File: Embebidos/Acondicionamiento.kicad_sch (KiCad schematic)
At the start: 20 parts

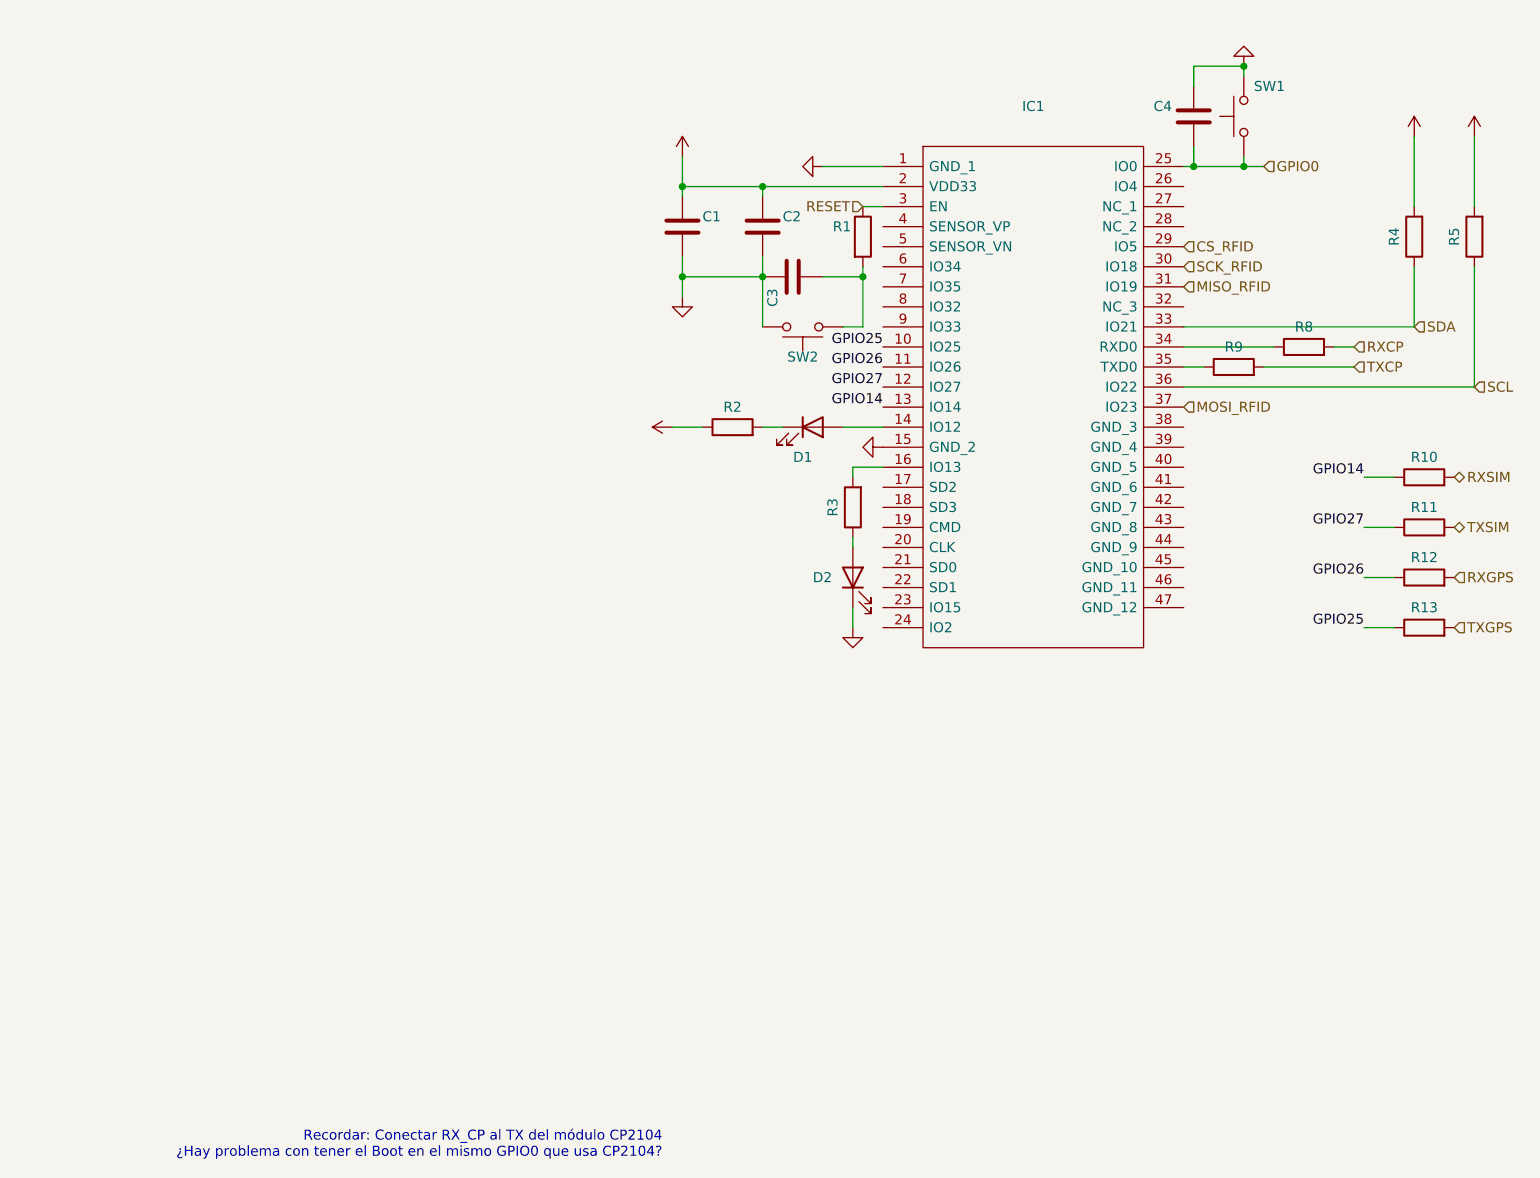
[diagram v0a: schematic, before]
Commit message: LDR module adittion
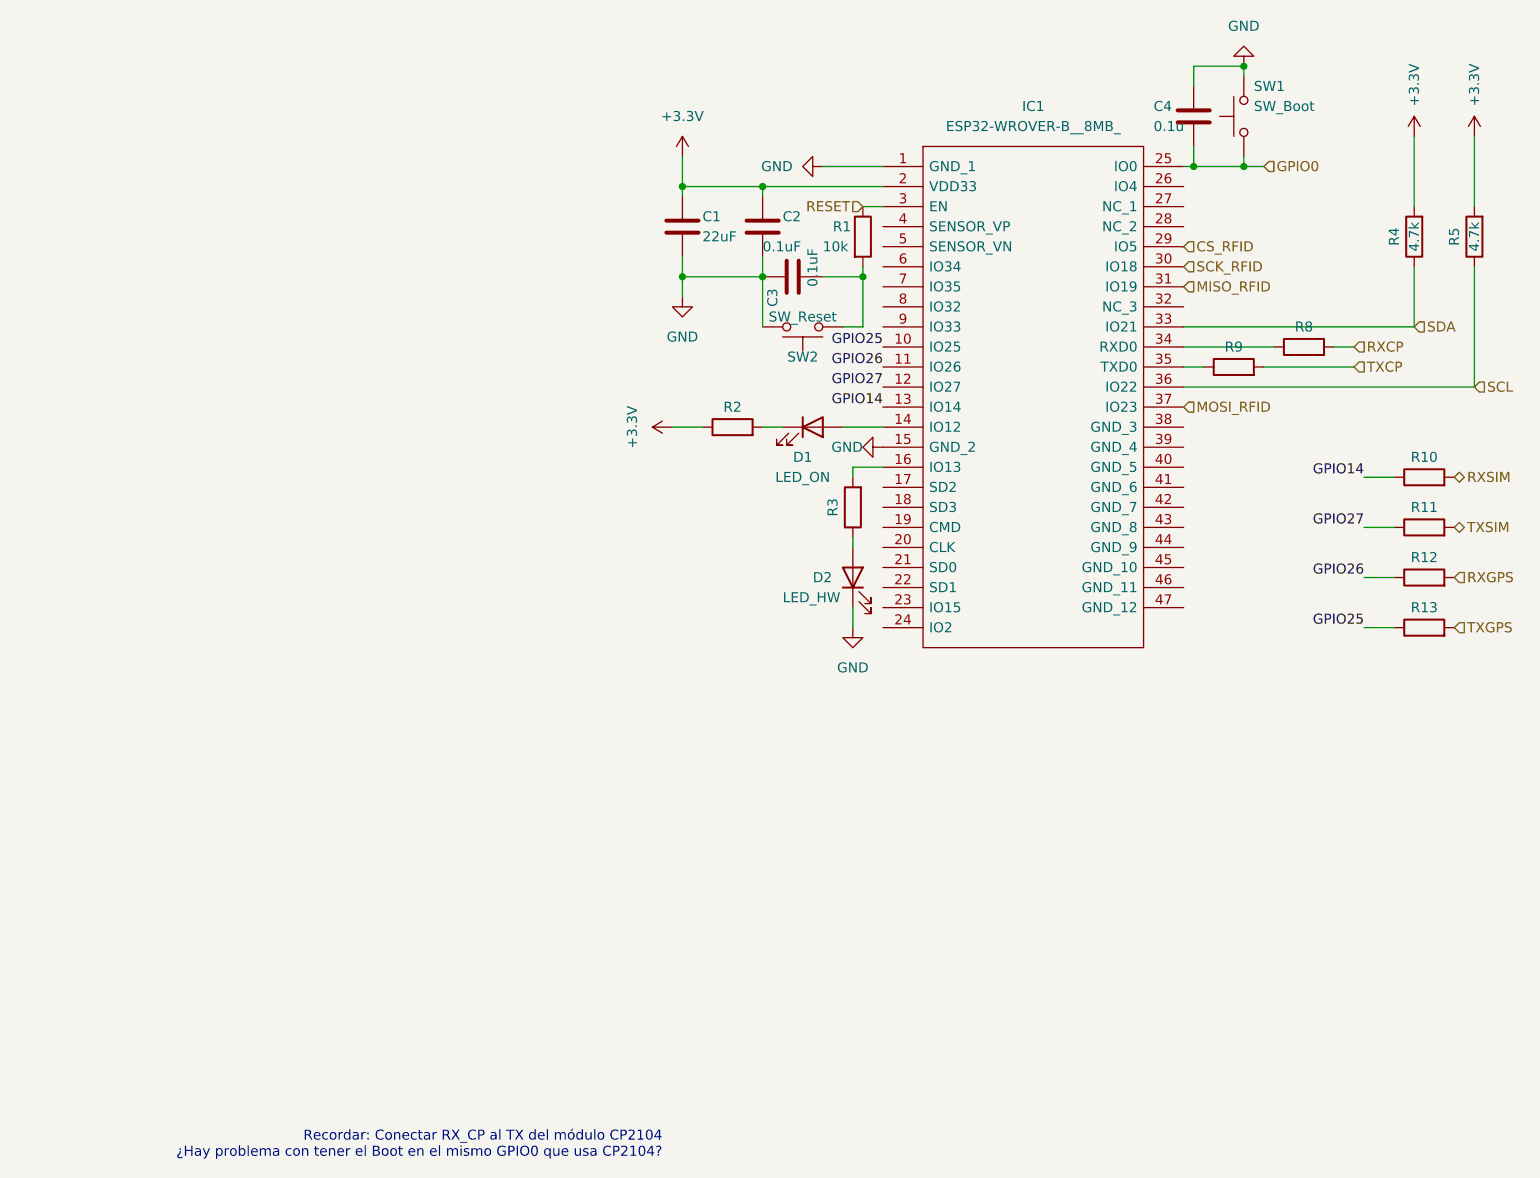
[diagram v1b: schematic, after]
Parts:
- C1: value (none) -> 22uF
- C2, C3: value (none) -> 0.1uF
- C4: value (none) -> 0.1u
- D1: value (none) -> LED_ON
- D2: value (none) -> LED_HW
- IC1: value (none) -> ESP32-WROVER-B__8MB_; footprint (none) -> ESP32WROVERB8MB
- R1: value (none) -> 10k
- R4, R5: value (none) -> 4.7k
- SW1: value (none) -> SW_Boot
- SW2: value (none) -> SW_Reset
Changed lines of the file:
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@@
       (effects (font (size 1.27 1.27)) (justify left))
     )
-    (property "Value" "" (id 1) (at 106.68 78.74 0)
+    (property "Value" "10k" (id 1) (at 106.68 78.74 0)
       (effects (font (size 1.27 1.27)) (justify left))
     )
@@
       (effects (font (size 1.27 1.27)) (justify left))
     )
-    (property "Value" "" (id 1) (at 105.41 83.82 0)
+    (property "Value" "0.1uF" (id 1) (at 105.41 83.82 0)
       (effects (font (size 1.27 1.27)) (justify left))
     )
@@
       (effects (font (size 1.27 1.27)) (justify left))
     )
-    (property "Value" "" (id 1) (at 99.06 78.74 0)
+    (property "Value" "0.1uF" (id 1) (at 99.06 78.74 0)
       (effects (font (size 1.27 1.27)) (justify left))
     )
@@
       (effects (font (size 1.27 1.27)) hide)
     )
-    (property "Value" "" (id 1) (at 88.9 90.17 0))
+    (property "Value" "GND" (id 1) (at 88.9 90.17 0))
     (property "Footprint" "" (id 2) (at 88.9 85.09 0)
       (effects (font (size 1.27 1.27)) hide)
@@
       (effects (font (size 1.27 1.27)) hide)
     )
-    (property "Value" "" (id 1) (at 160.02 50.8 0))
+    (property "Value" "GND" (id 1) (at 160.02 50.8 0))
     (property "Footprint" "" (id 2) (at 160.02 55.88 0)
       (effects (font (size 1.27 1.27)) hide)
@@
       (effects (font (size 1.27 1.27)) hide)
     )
-    (property "Value" "" (id 1) (at 111.76 104.14 90)
+    (property "Value" "GND" (id 1) (at 111.76 104.14 90)
       (effects (font (size 1.27 1.27)) (justify right))
     )
@@
       (effects (font (size 1.27 1.27)) hide)
     )
-    (property "Value" "" (id 1) (at 181.6099 60.96 90)
+    (property "Value" "+3.3V" (id 1) (at 181.6099 60.96 90)
       (effects (font (size 1.27 1.27)) (justify left))
     )
@@
       (effects (font (size 1.27 1.27)) (justify left))
     )
-    (property "Value" "" (id 1) (at 148.59 63.5 0)
+    (property "Value" "0.1u" (id 1) (at 148.59 63.5 0)
       (effects (font (size 1.27 1.27)) (justify left))
     )
@@
       (effects (font (size 1.27 1.27)) hide)
     )
-    (property "Value" "" (id 1) (at 88.9 62.23 0))
+    (property "Value" "+3.3V" (id 1) (at 88.9 62.23 0))
     (property "Footprint" "" (id 2) (at 88.9 67.31 0)
       (effects (font (size 1.27 1.27)) hide)
@@
       (effects (font (size 1.27 1.27)) (justify right))
     )
-    (property "Value" "" (id 1) (at 161.29 60.96 90)
+    (property "Value" "SW_Boot" (id 1) (at 161.29 60.96 90)
       (effects (font (size 1.27 1.27)) (justify right))
     )
@@
       (effects (font (size 1.27 1.27)) hide)
     )
-    (property "Value" "" (id 1) (at 189.2299 60.96 90)
+    (property "Value" "+3.3V" (id 1) (at 189.2299 60.96 90)
       (effects (font (size 1.27 1.27)) (justify left))
     )
@@
     (in_bom yes) (on_board yes)
     (property "Reference" "R4" (id 0) (at 179.07 77.47 90))
-    (property "Value" "" (id 1) (at 181.61 77.47 90))
+    (property "Value" "4.7k" (id 1) (at 181.61 77.47 90))
     (property "Footprint" "" (id 2) (at 183.388 77.47 90)
       (effects (font (size 1.27 1.27)) hide)
@@
       (effects (font (size 1.27 1.27)) hide)
     )
-    (property "Value" "" (id 1) (at 82.55 101.6 0))
+    (property "Value" "+3.3V" (id 1) (at 82.55 101.6 0))
     (property "Footprint" "" (id 2) (at 87.63 101.6 0)
       (effects (font (size 1.27 1.27)) hide)
@@
     (in_bom yes) (on_board yes)
     (property "Reference" "D1" (id 0) (at 104.14 105.41 0))
-    (property "Value" "" (id 1) (at 104.14 107.95 0))
+    (property "Value" "LED_ON" (id 1) (at 104.14 107.95 0))
     (property "Footprint" "" (id 2) (at 105.41 101.6 0)
       (effects (font (size 1.27 1.27)) hide)
@@
     (in_bom yes) (on_board yes)
     (property "Reference" "SW2" (id 0) (at 104.14 92.71 0))
-    (property "Value" "" (id 1) (at 104.14 87.63 0))
+    (property "Value" "SW_Reset" (id 1) (at 104.14 87.63 0))
     (property "Footprint" "" (id 2) (at 104.14 93.98 0)
       (effects (font (size 1.27 1.27)) hide)
@@
     (in_bom yes) (on_board yes) (fields_autoplaced)
     (property "Reference" "IC1" (id 0) (at 133.35 60.96 0))
-    (property "Value" "" (id 1) (at 133.35 63.5 0))
-    (property "Footprint" "" (id 2) (at 148.59 66.04 0)
+    (property "Value" "ESP32-WROVER-B__8MB_" (id 1) (at 133.35 63.5 0))
+    (property "Footprint" "ESP32WROVERB8MB" (id 2) (at 148.59 66.04 0)
       (effects (font (size 1.27 1.27)) (justify left) hide)
     )
@@
       (effects (font (size 1.27 1.27)) (justify left))
     )
-    (property "Value" "" (id 1) (at 91.44 77.47 0)
+    (property "Value" "22uF" (id 1) (at 91.44 77.47 0)
       (effects (font (size 1.27 1.27)) (justify left))
     )
@@
       (effects (font (size 1.27 1.27)) hide)
     )
-    (property "Value" "" (id 1) (at 102.87 68.5799 90)
+    (property "Value" "GND" (id 1) (at 102.87 68.5799 90)
       (effects (font (size 1.27 1.27)) (justify right))
     )
@@
     (in_bom yes) (on_board yes)
     (property "Reference" "R5" (id 0) (at 186.69 77.47 90))
-    (property "Value" "" (id 1) (at 189.23 77.47 90))
+    (property "Value" "4.7k" (id 1) (at 189.23 77.47 90))
     (property "Footprint" "" (id 2) (at 191.008 77.47 90)
       (effects (font (size 1.27 1.27)) hide)
@@
       (effects (font (size 1.27 1.27)) hide)
     )
-    (property "Value" "" (id 1) (at 110.49 132.08 0))
+    (property "Value" "GND" (id 1) (at 110.49 132.08 0))
     (property "Footprint" "" (id 2) (at 110.49 127 0)
       (effects (font (size 1.27 1.27)) hide)
@@
       (effects (font (size 1.27 1.27)) (justify right))
     )
-    (property "Value" "" (id 1) (at 101.6 123.19 90)
-      (effects (font (size 1.27 1.27)) (justify right))
-    )
+    (property "Value" "LED_HW" (id 1) (at 101.6 123.19 90)
+      (effects (font (size 1.27 1.27)) (justify right))
+    )

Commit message: Corrección de anotaciones
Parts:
- renumbered R2 to R1, R13 to R10, R5 to R11, R3 to R2, R1 to R3, R9 to R4, R8 to R5, R4 to R6, R10 to R7, R11 to R8, R12 to R9, SW2 to SW1, SW1 to SW2
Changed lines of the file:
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@@
   (symbol (lib_id "Device:R") (at 111.76 77.47 0) (unit 1)
     (in_bom yes) (on_board yes)
-    (property "Reference" "R1" (id 0) (at 107.95 76.2 0)
+    (property "Reference" "R3" (id 0) (at 107.95 76.2 0)
       (effects (font (size 1.27 1.27)) (justify left))
     )
@@
   (symbol (lib_id "Device:R") (at 158.75 93.98 90) (unit 1)
     (in_bom yes) (on_board yes)
-    (property "Reference" "R9" (id 0) (at 158.75 91.44 90))
+    (property "Reference" "R4" (id 0) (at 158.75 91.44 90))
     (property "Value" "~" (id 1) (at 158.75 93.98 90))
     (property "Footprint" "" (id 2) (at 158.75 95.758 90)
@@
   (symbol (lib_id "Device:R") (at 167.64 91.44 90) (unit 1)
     (in_bom yes) (on_board yes)
-    (property "Reference" "R8" (id 0) (at 167.64 88.9 90))
+    (property "Reference" "R5" (id 0) (at 167.64 88.9 90))
     (property "Value" "~" (id 1) (at 167.64 91.44 90))
     (property "Footprint" "" (id 2) (at 167.64 93.218 90)
@@
   (symbol (lib_id "Device:R") (at 110.49 111.76 180) (unit 1)
     (in_bom yes) (on_board yes)
-    (property "Reference" "R3" (id 0) (at 107.95 111.76 90))
+    (property "Reference" "R2" (id 0) (at 107.95 111.76 90))
     (property "Value" "~" (id 1) (at 110.49 111.76 90))
     (property "Footprint" "" (id 2) (at 112.268 111.76 90)
@@
   (symbol (lib_id "Device:R") (at 95.25 101.6 90) (unit 1)
     (in_bom yes) (on_board yes)
-    (property "Reference" "R2" (id 0) (at 95.25 99.06 90))
+    (property "Reference" "R1" (id 0) (at 95.25 99.06 90))
     (property "Value" "~" (id 1) (at 95.25 101.6 90))
     (property "Footprint" "" (id 2) (at 95.25 103.378 90)
@@
   (symbol (lib_id "power:GND") (at 88.9 85.09 0) (unit 1)
     (in_bom yes) (on_board yes) (fields_autoplaced)
-    (property "Reference" "#PWR?" (id 0) (at 88.9 91.44 0)
+    (property "Reference" "#PWR03" (id 0) (at 88.9 91.44 0)
       (effects (font (size 1.27 1.27)) hide)
     )
@@
   (symbol (lib_id "power:GND") (at 160.02 55.88 180) (unit 1)
     (in_bom yes) (on_board yes)
-    (property "Reference" "#PWR?" (id 0) (at 160.02 49.53 0)
+    (property "Reference" "#PWR07" (id 0) (at 160.02 49.53 0)
       (effects (font (size 1.27 1.27)) hide)
     )
@@
   (symbol (lib_id "power:GND") (at 114.3 104.14 270) (unit 1)
     (in_bom yes) (on_board yes)
-    (property "Reference" "#PWR?" (id 0) (at 107.95 104.14 0)
+    (property "Reference" "#PWR06" (id 0) (at 107.95 104.14 0)
       (effects (font (size 1.27 1.27)) hide)
     )
@@
   (symbol (lib_id "power:+3.3V") (at 181.61 64.77 0) (unit 1)
     (in_bom yes) (on_board yes)
-    (property "Reference" "#PWR?" (id 0) (at 181.61 68.58 0)
+    (property "Reference" "#PWR08" (id 0) (at 181.61 68.58 0)
       (effects (font (size 1.27 1.27)) hide)
     )
@@
   (symbol (lib_id "power:+3.3V") (at 88.9 67.31 0) (unit 1)
     (in_bom yes) (on_board yes) (fields_autoplaced)
-    (property "Reference" "#PWR?" (id 0) (at 88.9 71.12 0)
+    (property "Reference" "#PWR02" (id 0) (at 88.9 71.12 0)
       (effects (font (size 1.27 1.27)) hide)
     )
@@
   (symbol (lib_id "Switch:SW_Push") (at 160.02 62.23 90) (unit 1)
     (in_bom yes) (on_board yes)
-    (property "Reference" "SW1" (id 0) (at 161.29 58.42 90)
+    (property "Reference" "SW2" (id 0) (at 161.29 58.42 90)
       (effects (font (size 1.27 1.27)) (justify right))
     )
@@
   (symbol (lib_id "power:+3.3V") (at 189.23 64.77 0) (unit 1)
     (in_bom yes) (on_board yes) (fields_autoplaced)
-    (property "Reference" "#PWR?" (id 0) (at 189.23 68.58 0)
+    (property "Reference" "#PWR09" (id 0) (at 189.23 68.58 0)
       (effects (font (size 1.27 1.27)) hide)
     )
@@
   (symbol (lib_id "Device:R") (at 181.61 77.47 180) (unit 1)
     (in_bom yes) (on_board yes)
-    (property "Reference" "R4" (id 0) (at 179.07 77.47 90))
+    (property "Reference" "R6" (id 0) (at 179.07 77.47 90))
     (property "Value" "4.7k" (id 1) (at 181.61 77.47 90))
     (property "Footprint" "" (id 2) (at 183.388 77.47 90)
@@
   (symbol (lib_id "power:+3.3V") (at 87.63 101.6 90) (unit 1)
     (in_bom yes) (on_board yes)
-    (property "Reference" "#PWR?" (id 0) (at 91.44 101.6 0)
+    (property "Reference" "#PWR01" (id 0) (at 91.44 101.6 0)
       (effects (font (size 1.27 1.27)) hide)
     )
@@
   (symbol (lib_id "Device:R") (at 182.88 120.65 90) (unit 1)
     (in_bom yes) (on_board yes)
-    (property "Reference" "R12" (id 0) (at 182.88 118.11 90))
+    (property "Reference" "R9" (id 0) (at 182.88 118.11 90))
     (property "Value" "~" (id 1) (at 182.88 120.65 90))
     (property "Footprint" "" (id 2) (at 182.88 122.428 90)
@@
   (symbol (lib_id "Switch:SW_MEC_5G") (at 104.14 88.9 180) (unit 1)
     (in_bom yes) (on_board yes)
-    (property "Reference" "SW2" (id 0) (at 104.14 92.71 0))
+    (property "Reference" "SW1" (id 0) (at 104.14 92.71 0))
     (property "Value" "SW_Reset" (id 1) (at 104.14 87.63 0))
     (property "Footprint" "" (id 2) (at 104.14 93.98 0)
@@
   (symbol (lib_id "Device:R") (at 182.88 107.95 90) (unit 1)
     (in_bom yes) (on_board yes)
-    (property "Reference" "R10" (id 0) (at 182.88 105.41 90))
+    (property "Reference" "R7" (id 0) (at 182.88 105.41 90))
     (property "Value" "~" (id 1) (at 182.88 107.95 90))
     (property "Footprint" "" (id 2) (at 182.88 109.728 90)
@@
   (symbol (lib_id "power:GND") (at 106.68 68.58 270) (unit 1)
     (in_bom yes) (on_board yes) (fields_autoplaced)
-    (property "Reference" "#PWR?" (id 0) (at 100.33 68.58 0)
+    (property "Reference" "#PWR04" (id 0) (at 100.33 68.58 0)
       (effects (font (size 1.27 1.27)) hide)
     )
@@
   (symbol (lib_id "Device:R") (at 182.88 114.3 90) (unit 1)
     (in_bom yes) (on_board yes)
-    (property "Reference" "R11" (id 0) (at 182.88 111.76 90))
+    (property "Reference" "R8" (id 0) (at 182.88 111.76 90))
     (property "Value" "~" (id 1) (at 182.88 114.3 90))
     (property "Footprint" "" (id 2) (at 182.88 116.078 90)
@@
   (symbol (lib_id "Device:R") (at 182.88 127 90) (unit 1)
     (in_bom yes) (on_board yes)
-    (property "Reference" "R13" (id 0) (at 182.88 124.46 90))
+    (property "Reference" "R10" (id 0) (at 182.88 124.46 90))
     (property "Value" "~" (id 1) (at 182.88 127 90))
     (property "Footprint" "" (id 2) (at 182.88 128.778 90)
@@
   (symbol (lib_id "Device:R") (at 189.23 77.47 180) (unit 1)
     (in_bom yes) (on_board yes)
-    (property "Reference" "R5" (id 0) (at 186.69 77.47 90))
+    (property "Reference" "R11" (id 0) (at 186.69 77.47 90))
     (property "Value" "4.7k" (id 1) (at 189.23 77.47 90))
     (property "Footprint" "" (id 2) (at 191.008 77.47 90)
@@
   (symbol (lib_id "power:GND") (at 110.49 127 0) (unit 1)
     (in_bom yes) (on_board yes) (fields_autoplaced)
-    (property "Reference" "#PWR?" (id 0) (at 110.49 133.35 0)
-      (effects (font (size 1.27 1.27)) hide)
-    )
+    (property "Reference" "#PWR05" (id 0) (at 110.49 133.35 0)
+      (effects (font (size 1.27 1.27)) hide)
+    )
